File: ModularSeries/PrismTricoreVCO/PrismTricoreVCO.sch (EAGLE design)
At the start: 58 parts, among them Q1 2N3906, Q2 2N3906

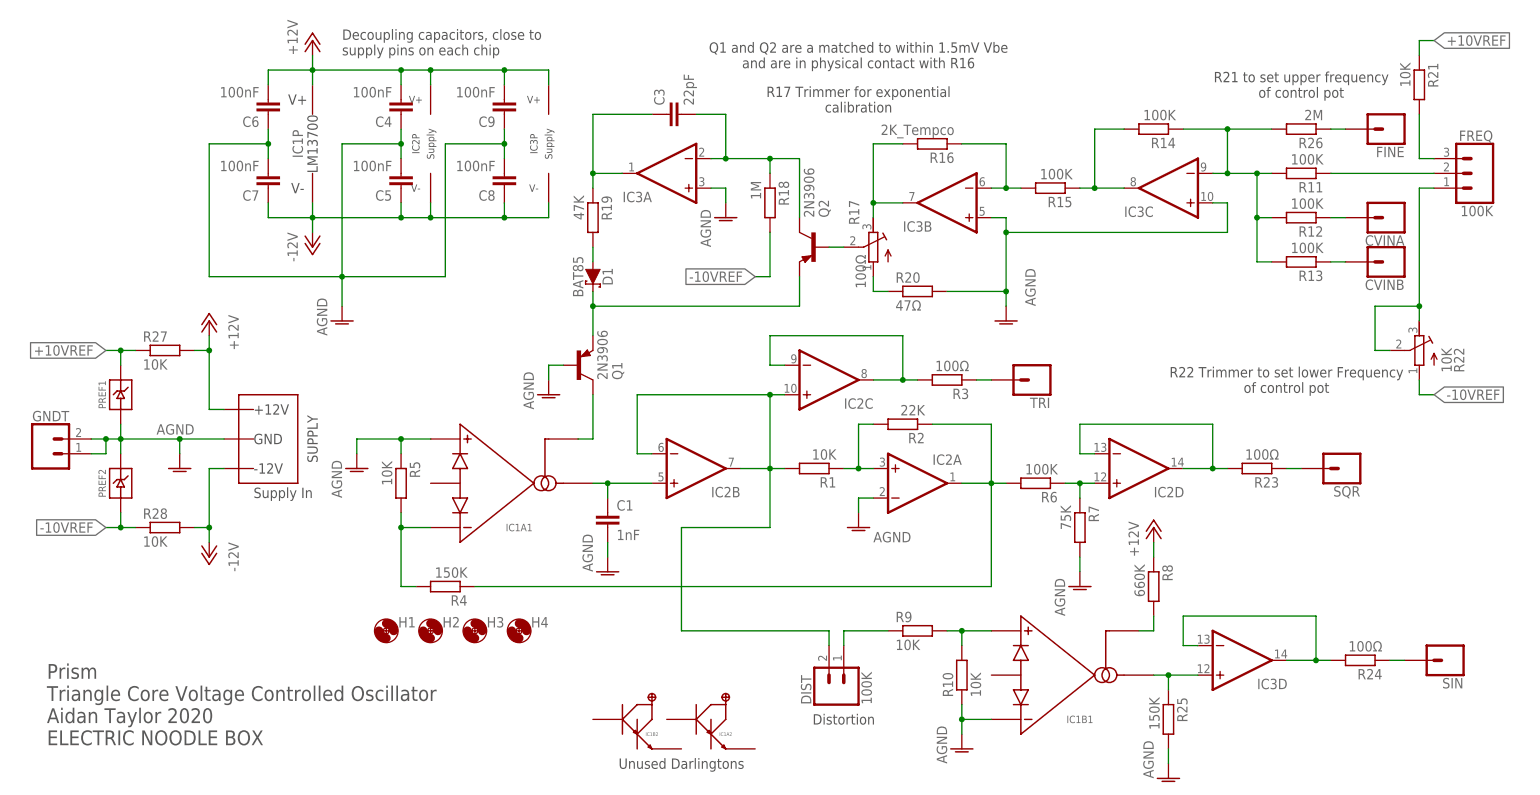
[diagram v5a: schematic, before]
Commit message: Prism updates, silkscreen errors fixed, resistor values updated, BOM updated
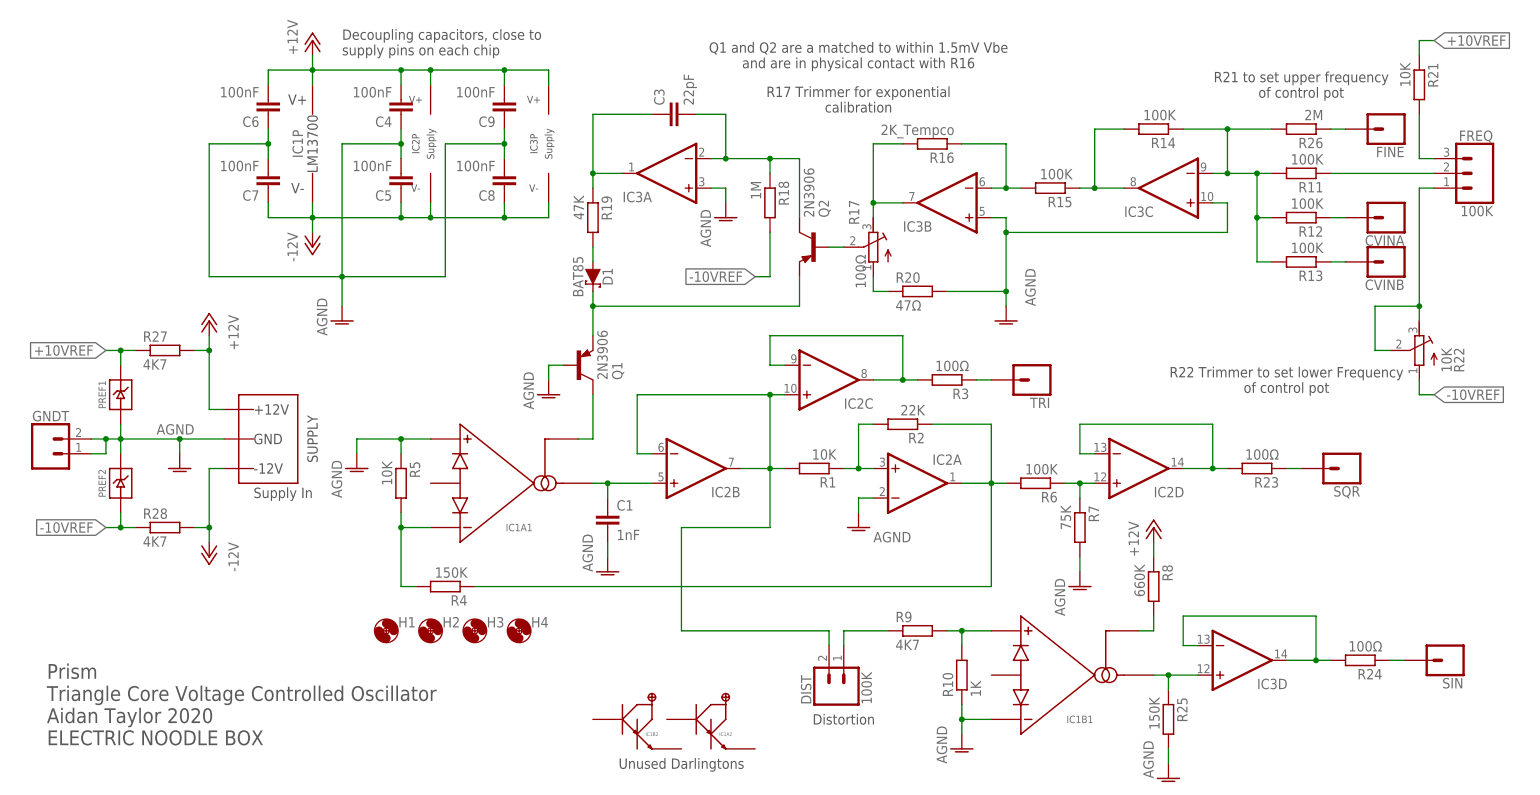
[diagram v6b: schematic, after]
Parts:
- R10: value 10K -> 1K
- R27, R28, R9: value 10K -> 4K7
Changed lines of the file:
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@@
 <part name="AGND7" library="supply1" library_urn="urn:adsk.eagle:library:371" deviceset="AGND" device=""/>
 <part name="R8" library="rcl" library_urn="urn:adsk.eagle:library:334" deviceset="R-EU_" device="0207/10" package3d_urn="urn:adsk.eagle:package:23491/2" value="660K"/>
-<part name="R9" library="rcl" library_urn="urn:adsk.eagle:library:334" deviceset="R-EU_" device="0207/10" package3d_urn="urn:adsk.eagle:package:23491/2" value="10K"/>
-<part name="R10" library="rcl" library_urn="urn:adsk.eagle:library:334" deviceset="R-EU_" device="0207/10" package3d_urn="urn:adsk.eagle:package:23491/2" value="10K"/>
+<part name="R9" library="rcl" library_urn="urn:adsk.eagle:library:334" deviceset="R-EU_" device="0207/10" package3d_urn="urn:adsk.eagle:package:23491/2" value="4K7"/>
+<part name="R10" library="rcl" library_urn="urn:adsk.eagle:library:334" deviceset="R-EU_" device="0207/10" package3d_urn="urn:adsk.eagle:package:23491/2" value="1K"/>
 <part name="AGND2" library="supply1" library_urn="urn:adsk.eagle:library:371" deviceset="AGND" device=""/>
 <part name="P+1" library="supply1" library_urn="urn:adsk.eagle:library:371" deviceset="+12V" device=""/>
@@
 <part name="PREF1" library="ElectricNoodleBox" deviceset="LM4040" device="TH"/>
 <part name="PREF2" library="ElectricNoodleBox" deviceset="LM4040" device="TH"/>
-<part name="R27" library="rcl" library_urn="urn:adsk.eagle:library:334" deviceset="R-EU_" device="0207/10" package3d_urn="urn:adsk.eagle:package:23491/2" value="10K"/>
-<part name="R28" library="rcl" library_urn="urn:adsk.eagle:library:334" deviceset="R-EU_" device="0207/10" package3d_urn="urn:adsk.eagle:package:23491/2" value="10K"/>
+<part name="R27" library="rcl" library_urn="urn:adsk.eagle:library:334" deviceset="R-EU_" device="0207/10" package3d_urn="urn:adsk.eagle:package:23491/2" value="4K7"/>
+<part name="R28" library="rcl" library_urn="urn:adsk.eagle:library:334" deviceset="R-EU_" device="0207/10" package3d_urn="urn:adsk.eagle:package:23491/2" value="4K7"/>
 </parts>
 <sheets>
